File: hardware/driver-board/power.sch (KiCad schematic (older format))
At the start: 3 parts, among them U2 AIC1748

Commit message: Rework power to four different voltage domains
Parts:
- removed U2: AIC1748, Package_TO_SOT_SMD:SOT-23, symbol driver-board:AIC1748
- added C5, C6: 10µF, Capacitor_SMD:C_0603_1608Metric, symbol Device:C
- added C7: 1µF, Capacitor_SMD:C_0603_1608Metric, symbol Device:C
- added C8: 4.7µF, Capacitor_SMD:C_0603_1608Metric, symbol Device:C
- added L1: 10µH, Inductor_SMD:L_0603_1608Metric, symbol Device:L
- added R1: 1M, Resistor_SMD:R_0603_1608Metric, symbol Device:R
- added R2: 71.5k, Resistor_SMD:R_0603_1608Metric, symbol Device:R
- added U2, U3: ME6210, Package_TO_SOT_SMD:SOT-23, symbol driver-board:ME6210
- added U4: TLV61046ADB, Package_TO_SOT_SMD:SOT-23-6, symbol Regulator_Switching:TLV61046ADB
- C3, C4: value 1µF -> 10µF
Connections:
- net labels added: +12V, +3V0
- wire segments 5 -> 16

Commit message: Add display schematics
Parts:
- renumbered C5 to C3, C6 to C4, C3 to C5, C4 to C6, U3 to U2, U2 to U3
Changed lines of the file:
@@
 $Descr A4 11693 8268
 encoding utf-8
-Sheet 3 6
+Sheet 3 7
 Title "FT81x TFT040 Driver Board"
-Date "2020-07-03"
+Date "2020-07-05"
 Rev "2007D"
 Comp ""
@@
 $EndDescr
 $Comp
-L driver-board:ME6210 U2
+L driver-board:ME6210 U3
 U 1 1 5F050907
 P 4150 2150
-F 0 "U2" H 4150 2565 50  0000 C CNN
+F 0 "U3" H 4150 2565 50  0000 C CNN
 F 1 "ME6210" H 4150 2474 50  0000 C CNN
 F 2 "Package_TO_SOT_SMD:SOT-23" H 4150 1400 50  0001 C CNN
@@
 $EndComp
 $Comp
-L driver-board:ME6210 U3
+L driver-board:ME6210 U2
 U 1 1 5F051BDD
 P 7200 2100
-F 0 "U3" H 7200 2515 50  0000 C CNN
+F 0 "U2" H 7200 2515 50  0000 C CNN
 F 1 "ME6210" H 7200 2424 50  0000 C CNN
 F 2 "Package_TO_SOT_SMD:SOT-23" H 7200 1350 50  0001 C CNN
@@
 $EndComp
 $Comp
-L Device:C C3
+L Device:C C5
 U 1 1 5F05254D
 P 3500 2200
-F 0 "C3" H 3615 2246 50  0000 L CNN
+F 0 "C5" H 3615 2246 50  0000 L CNN
 F 1 "10µF" H 3615 2155 50  0000 L CNN
 F 2 "Capacitor_SMD:C_0603_1608Metric" H 3538 2050 50  0001 C CNN
@@
 $EndComp
 $Comp
-L Device:C C4
+L Device:C C6
 U 1 1 5F052D97
 P 4800 2200
-F 0 "C4" H 4915 2246 50  0000 L CNN
+F 0 "C6" H 4915 2246 50  0000 L CNN
 F 1 "10µF" H 4915 2155 50  0000 L CNN
 F 2 "Capacitor_SMD:C_0603_1608Metric" H 4838 2050 50  0001 C CNN
@@
 	3800 2050 3500 2050
 $Comp
-L power:GND #PWR017
+L power:GND #PWR018
 U 1 1 5F0548F7
 P 4150 2400
-F 0 "#PWR017" H 4150 2150 50  0001 C CNN
+F 0 "#PWR018" H 4150 2150 50  0001 C CNN
 F 1 "GND" H 4155 2227 50  0000 C CNN
 F 2 "" H 4150 2400 50  0001 C CNN
@@
 $EndComp
 $Comp
-L power:GND #PWR013
+L power:GND #PWR015
 U 1 1 5F055174
 P 3500 2350
-F 0 "#PWR013" H 3500 2100 50  0001 C CNN
+F 0 "#PWR015" H 3500 2100 50  0001 C CNN
 F 1 "GND" H 3505 2177 50  0000 C CNN
 F 2 "" H 3500 2350 50  0001 C CNN
@@
 $EndComp
 $Comp
-L power:GND #PWR014
+L power:GND #PWR016
 U 1 1 5F055676
 P 4800 2350
-F 0 "#PWR014" H 4800 2100 50  0001 C CNN
+F 0 "#PWR016" H 4800 2100 50  0001 C CNN
 F 1 "GND" H 4805 2177 50  0000 C CNN
 F 2 "" H 4800 2350 50  0001 C CNN
@@
 $EndComp
 $Comp
-L power:+3.3V #PWR010
+L power:+3.3V #PWR012
 U 1 1 5F055D4A
 P 4800 2050
-F 0 "#PWR010" H 4800 1900 50  0001 C CNN
+F 0 "#PWR012" H 4800 1900 50  0001 C CNN
 F 1 "+3.3V" H 4815 2223 50  0000 C CNN
 F 2 "" H 4800 2050 50  0001 C CNN
@@
 Connection ~ 4800 2050
 $Comp
-L power:+5V #PWR09
+L power:+5V #PWR011
 U 1 1 5F056439
 P 3500 2050
-F 0 "#PWR09" H 3500 1900 50  0001 C CNN
+F 0 "#PWR011" H 3500 1900 50  0001 C CNN
 F 1 "+5V" H 3515 2223 50  0000 C CNN
 F 2 "" H 3500 2050 50  0001 C CNN
@@
 Connection ~ 3500 2050
 $Comp
-L Device:C C5
+L Device:C C3
 U 1 1 5F057FFE
 P 6550 2150
-F 0 "C5" H 6665 2196 50  0000 L CNN
+F 0 "C3" H 6665 2196 50  0000 L CNN
 F 1 "10µF" H 6665 2105 50  0000 L CNN
 F 2 "Capacitor_SMD:C_0603_1608Metric" H 6588 2000 50  0001 C CNN
@@
 $EndComp
 $Comp
-L Device:C C6
+L Device:C C4
 U 1 1 5F058C7E
 P 7850 2150
-F 0 "C6" H 7965 2196 50  0000 L CNN
+F 0 "C4" H 7965 2196 50  0000 L CNN
 F 1 "10µF" H 7965 2105 50  0000 L CNN
 F 2 "Capacitor_SMD:C_0603_1608Metric" H 7888 2000 50  0001 C CNN
@@
 	7550 2000 7850 2000
 $Comp
-L power:GND #PWR016
+L power:GND #PWR014
 U 1 1 5F05A343
 P 7850 2300
-F 0 "#PWR016" H 7850 2050 50  0001 C CNN
+F 0 "#PWR014" H 7850 2050 50  0001 C CNN
 F 1 "GND" H 7855 2127 50  0000 C CNN
 F 2 "" H 7850 2300 50  0001 C CNN
@@
 $EndComp
 $Comp
-L power:GND #PWR018
+L power:GND #PWR017
 U 1 1 5F05A491
 P 7200 2350
-F 0 "#PWR018" H 7200 2100 50  0001 C CNN
+F 0 "#PWR017" H 7200 2100 50  0001 C CNN
 F 1 "GND" H 7205 2177 50  0000 C CNN
 F 2 "" H 7200 2350 50  0001 C CNN
@@
 $EndComp
 $Comp
-L power:GND #PWR015
+L power:GND #PWR013
 U 1 1 5F05A5EB
 P 6550 2300
-F 0 "#PWR015" H 6550 2050 50  0001 C CNN
+F 0 "#PWR013" H 6550 2050 50  0001 C CNN
 F 1 "GND" H 6555 2127 50  0000 C CNN
 F 2 "" H 6550 2300 50  0001 C CNN
@@
 $EndComp
 $Comp
-L power:+5V #PWR011
+L power:+5V #PWR09
 U 1 1 5F05A77C
 P 6550 2000
-F 0 "#PWR011" H 6550 1850 50  0001 C CNN
+F 0 "#PWR09" H 6550 1850 50  0001 C CNN
 F 1 "+5V" H 6565 2173 50  0000 C CNN
 F 2 "" H 6550 2000 50  0001 C CNN
@@
 Connection ~ 6550 2000
 $Comp
-L power:+3V0 #PWR012
+L power:+3V0 #PWR010
 U 1 1 5F05A91B
 P 7850 2000
-F 0 "#PWR012" H 7850 1850 50  0001 C CNN
+F 0 "#PWR010" H 7850 1850 50  0001 C CNN
 F 1 "+3V0" H 7865 2173 50  0000 C CNN
 F 2 "" H 7850 2000 50  0001 C CNN

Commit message: Improve and fix pcb and schematic
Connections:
- net +12V: now also U4.5 (VOUT); no longer R2.1, U4.3 (FB)
- net at R1.2: now also R2.1, U4.3 (FB); no longer U4.5 (VOUT)
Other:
- moved on the sheet: C8, R2
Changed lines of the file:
@@
 $EndComp
-$Comp
-L Device:R R1
-U 1 1 5F06FAA8
-P 6350 4250
-F 0 "R1" V 6250 4250 50  0000 C CNN
-F 1 "1M" V 6350 4250 50  0000 C CNN
-F 2 "Resistor_SMD:R_0603_1608Metric" V 6280 4250 50  0001 C CNN
-F 3 "~" H 6350 4250 50  0001 C CNN
-	1    6350 4250
-	0    1    1    0
-$EndComp
-Wire Wire Line
-	6050 4250 6200 4250
 $Comp
 L Device:R R2
 U 1 1 5F07151B
-P 6500 4600
-F 0 "R2" H 6570 4646 50  0000 L CNN
-F 1 "71.5k" H 6570 4555 50  0000 L CNN
-F 2 "Resistor_SMD:R_0603_1608Metric" V 6430 4600 50  0001 C CNN
-F 3 "~" H 6500 4600 50  0001 C CNN
-	1    6500 4600
+P 6400 4800
+F 0 "R2" H 6470 4846 50  0000 L CNN
+F 1 "71.5k" H 6470 4755 50  0000 L CNN
+F 2 "Resistor_SMD:R_0603_1608Metric" V 6330 4800 50  0001 C CNN
+F 3 "~" H 6400 4800 50  0001 C CNN
+	1    6400 4800
 	1    0    0    -1
 $EndComp
-Wire Wire Line
-	6500 4250 6500 4350
-Wire Wire Line
-	6050 4350 6500 4350
-Connection ~ 6500 4350
-Wire Wire Line
-	6500 4350 6500 4450
 $Comp
 L power:GND #PWR025
 U 1 1 5F072953
-P 6500 4750
-F 0 "#PWR025" H 6500 4500 50  0001 C CNN
-F 1 "GND" H 6505 4577 50  0000 C CNN
-F 2 "" H 6500 4750 50  0001 C CNN
-F 3 "" H 6500 4750 50  0001 C CNN
-	1    6500 4750
+P 6400 4950
+F 0 "#PWR025" H 6400 4700 50  0001 C CNN
+F 1 "GND" H 6405 4777 50  0000 C CNN
+F 2 "" H 6400 4950 50  0001 C CNN
+F 3 "" H 6400 4950 50  0001 C CNN
+	1    6400 4950
 	1    0    0    -1
 $EndComp
@@
 L Device:C C8
 U 1 1 5F07504E
-P 7000 4400
-F 0 "C8" H 7115 4446 50  0000 L CNN
-F 1 "4.7µF" H 7115 4355 50  0000 L CNN
-F 2 "Capacitor_SMD:C_0603_1608Metric" H 7038 4250 50  0001 C CNN
-F 3 "~" H 7000 4400 50  0001 C CNN
-	1    7000 4400
+P 6800 4400
+F 0 "C8" H 6915 4446 50  0000 L CNN
+F 1 "4.7µF" H 6915 4355 50  0000 L CNN
+F 2 "Capacitor_SMD:C_0603_1608Metric" H 6838 4250 50  0001 C CNN
+F 3 "~" H 6800 4400 50  0001 C CNN
+	1    6800 4400
 	1    0    0    -1
 $EndComp
-Wire Wire Line
-	6500 4250 7000 4250
-Connection ~ 6500 4250
 $Comp
 L power:GND #PWR024
 U 1 1 5F076C9E
-P 7000 4550
-F 0 "#PWR024" H 7000 4300 50  0001 C CNN
-F 1 "GND" H 7005 4377 50  0000 C CNN
-F 2 "" H 7000 4550 50  0001 C CNN
-F 3 "" H 7000 4550 50  0001 C CNN
-	1    7000 4550
+P 6800 4550
+F 0 "#PWR024" H 6800 4300 50  0001 C CNN
+F 1 "GND" H 6805 4377 50  0000 C CNN
+F 2 "" H 6800 4550 50  0001 C CNN
+F 3 "" H 6800 4550 50  0001 C CNN
+	1    6800 4550
 	1    0    0    -1
 $EndComp
@@
 L power:+12V #PWR020
 U 1 1 5F07735E
-P 7000 4250
-F 0 "#PWR020" H 7000 4100 50  0001 C CNN
-F 1 "+12V" H 7015 4423 50  0000 C CNN
-F 2 "" H 7000 4250 50  0001 C CNN
-F 3 "" H 7000 4250 50  0001 C CNN
-	1    7000 4250
+P 6800 4250
+F 0 "#PWR020" H 6800 4100 50  0001 C CNN
+F 1 "+12V" H 6815 4423 50  0000 C CNN
+F 2 "" H 6800 4250 50  0001 C CNN
+F 3 "" H 6800 4250 50  0001 C CNN
+	1    6800 4250
 	1    0    0    -1
 $EndComp
-Connection ~ 7000 4250
 $Comp
 L Device:L L1
@@
 Wire Wire Line
 	5350 4150 4800 4150
+$Comp
+L Device:R R1
+U 1 1 5F0697E7
+P 6400 4400
+F 0 "R1" H 6470 4446 50  0000 L CNN
+F 1 "1M" H 6470 4355 50  0000 L CNN
+F 2 "Resistor_SMD:R_0603_1608Metric" V 6330 4400 50  0001 C CNN
+F 3 "~" H 6400 4400 50  0001 C CNN
+	1    6400 4400
+	1    0    0    -1
+$EndComp
+Wire Wire Line
+	6050 4250 6400 4250
+Connection ~ 6800 4250
+Connection ~ 6400 4250
+Wire Wire Line
+	6400 4250 6800 4250
+Wire Wire Line
+	6400 4550 6400 4600
+Wire Wire Line
+	6050 4350 6150 4350
+Wire Wire Line
+	6150 4350 6150 4600
+Wire Wire Line
+	6150 4600 6400 4600
+Connection ~ 6400 4600
+Wire Wire Line
+	6400 4600 6400 4650
 $EndSCHEMATC

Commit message: Add missing JLCPCB part numbers
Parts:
- C3, C4, C5, C6: JLCPCB (none) -> C19702
- C7: JLCPCB (none) -> C15849
- R2: JLCPCB (none) -> C23103
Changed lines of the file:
@@
 F 2 "Capacitor_SMD:C_0603_1608Metric" H 3538 2050 50  0001 C CNN
 F 3 "~" H 3500 2200 50  0001 C CNN
+F 4 "C19702" H 3500 2200 50  0001 C CNN "JLCPCB"
 	1    3500 2200
 	1    0    0    -1
@@
 F 2 "Capacitor_SMD:C_0603_1608Metric" H 4838 2050 50  0001 C CNN
 F 3 "~" H 4800 2200 50  0001 C CNN
+F 4 "C19702" H 4800 2200 50  0001 C CNN "JLCPCB"
 	1    4800 2200
 	1    0    0    -1
@@
 F 2 "Capacitor_SMD:C_0603_1608Metric" H 6588 2000 50  0001 C CNN
 F 3 "~" H 6550 2150 50  0001 C CNN
+F 4 "C19702" H 6550 2150 50  0001 C CNN "JLCPCB"
 	1    6550 2150
 	1    0    0    -1
@@
 F 2 "Capacitor_SMD:C_0603_1608Metric" H 7888 2000 50  0001 C CNN
 F 3 "~" H 7850 2150 50  0001 C CNN
+F 4 "C19702" H 7850 2150 50  0001 C CNN "JLCPCB"
 	1    7850 2150
 	1    0    0    -1
@@
 F 2 "Capacitor_SMD:C_0603_1608Metric" H 4838 4150 50  0001 C CNN
 F 3 "~" H 4800 4300 50  0001 C CNN
+F 4 "C15849" H 4800 4300 50  0001 C CNN "JLCPCB"
 	1    4800 4300
 	1    0    0    -1
@@
 F 2 "Resistor_SMD:R_0603_1608Metric" V 6330 4800 50  0001 C CNN
 F 3 "~" H 6400 4800 50  0001 C CNN
+F 4 "C23103" H 6400 4800 50  0001 C CNN "JLCPCB"
 	1    6400 4800
 	1    0    0    -1

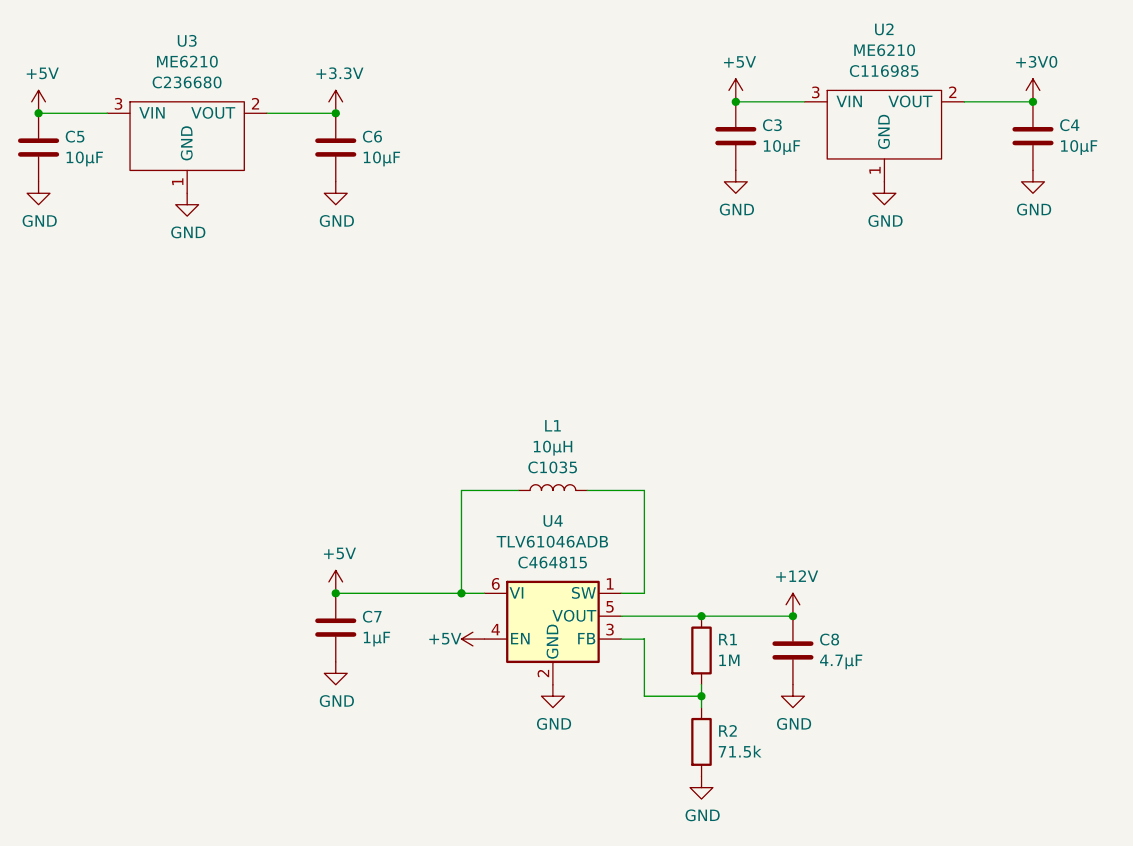
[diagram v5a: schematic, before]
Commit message: Rename JLCPCB to LCSC and update PCB
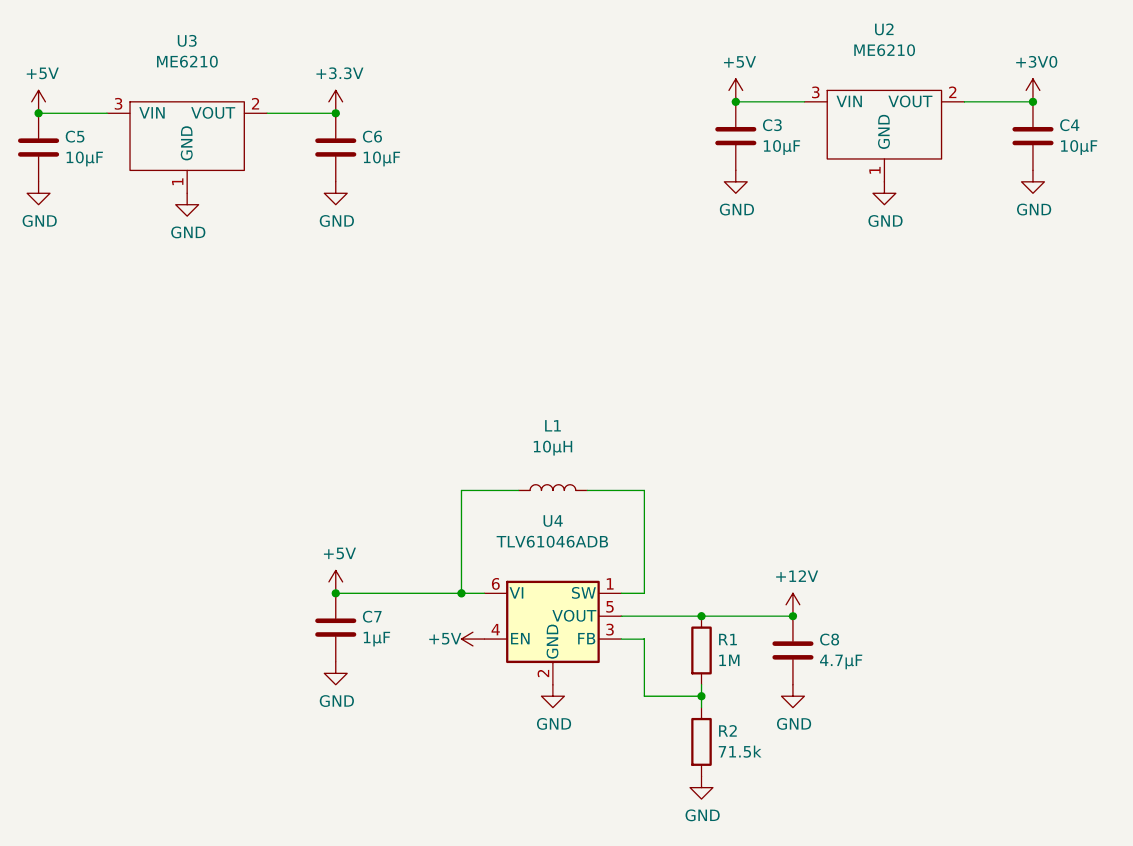
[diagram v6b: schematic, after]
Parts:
- C3, C4, C5, C6: JLCPCB C19702 -> (none); LCSC (none) -> C19702
- C7: JLCPCB C15849 -> (none); LCSC (none) -> C15849
- C8: LCSC (none) -> C19666
- L1: JLCPCB C1035 -> (none); LCSC (none) -> C1035
- R1: LCSC (none) -> C22935
- R2: JLCPCB C23103 -> (none); LCSC (none) -> C23103
- U2: JLCPCB C116985 -> (none); LCSC (none) -> C116985
- U3: JLCPCB C236680 -> (none); LCSC (none) -> C236680
- U4: JLCPCB C464815 -> (none); LCSC (none) -> C464815
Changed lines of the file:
@@
 F 2 "Package_TO_SOT_SMD:SOT-23" H 4150 1400 50  0001 C CNN
 F 3 "" H 4150 2150 50  0001 C CNN
-F 4 "C236680" H 4150 2383 50  0000 C CNN "JLCPCB"
+F 4 "C236680" H 4150 2150 50  0001 C CNN "LCSC"
 	1    4150 2150
 	1    0    0    -1
@@
 F 2 "Package_TO_SOT_SMD:SOT-23" H 7200 1350 50  0001 C CNN
 F 3 "" H 7200 2100 50  0001 C CNN
-F 4 "C116985" H 7200 2333 50  0000 C CNN "JLCPCB"
+F 4 "C116985" H 7200 2100 50  0001 C CNN "LCSC"
 	1    7200 2100
 	1    0    0    -1
@@
 F 2 "Capacitor_SMD:C_0603_1608Metric" H 3538 2050 50  0001 C CNN
 F 3 "~" H 3500 2200 50  0001 C CNN
-F 4 "C19702" H 3500 2200 50  0001 C CNN "JLCPCB"
+F 4 "C19702" H 3500 2200 50  0001 C CNN "LCSC"
 	1    3500 2200
 	1    0    0    -1
@@
 F 2 "Capacitor_SMD:C_0603_1608Metric" H 4838 2050 50  0001 C CNN
 F 3 "~" H 4800 2200 50  0001 C CNN
-F 4 "C19702" H 4800 2200 50  0001 C CNN "JLCPCB"
+F 4 "C19702" H 4800 2200 50  0001 C CNN "LCSC"
 	1    4800 2200
 	1    0    0    -1
@@
 F 2 "Capacitor_SMD:C_0603_1608Metric" H 6588 2000 50  0001 C CNN
 F 3 "~" H 6550 2150 50  0001 C CNN
-F 4 "C19702" H 6550 2150 50  0001 C CNN "JLCPCB"
+F 4 "C19702" H 6550 2150 50  0001 C CNN "LCSC"
 	1    6550 2150
 	1    0    0    -1
@@
 F 2 "Capacitor_SMD:C_0603_1608Metric" H 7888 2000 50  0001 C CNN
 F 3 "~" H 7850 2150 50  0001 C CNN
-F 4 "C19702" H 7850 2150 50  0001 C CNN "JLCPCB"
+F 4 "C19702" H 7850 2150 50  0001 C CNN "LCSC"
 	1    7850 2150
 	1    0    0    -1
@@
 F 2 "Package_TO_SOT_SMD:SOT-23-6" H 5800 4200 50  0001 L CIN
 F 3 "http://www.ti.com/lit/ds/symlink/tlv61046a.pdf" H 5750 4450 50  0001 C CNN
-F 4 "C464815" H 5750 4683 50  0000 C CNN "JLCPCB"
+F 4 "C464815" H 5750 4350 50  0001 C CNN "LCSC"
 	1    5750 4350
 	1    0    0    -1
@@
 F 2 "Capacitor_SMD:C_0603_1608Metric" H 4838 4150 50  0001 C CNN
 F 3 "~" H 4800 4300 50  0001 C CNN
-F 4 "C15849" H 4800 4300 50  0001 C CNN "JLCPCB"
+F 4 "C15849" H 4800 4300 50  0001 C CNN "LCSC"
 	1    4800 4300
 	1    0    0    -1
@@
 F 2 "Resistor_SMD:R_0603_1608Metric" V 6330 4800 50  0001 C CNN
 F 3 "~" H 6400 4800 50  0001 C CNN
-F 4 "C23103" H 6400 4800 50  0001 C CNN "JLCPCB"
+F 4 "C23103" H 6400 4800 50  0001 C CNN "LCSC"
 	1    6400 4800
 	1    0    0    -1
@@
 F 2 "Capacitor_SMD:C_0603_1608Metric" H 6838 4250 50  0001 C CNN
 F 3 "~" H 6800 4400 50  0001 C CNN
+F 4 "C19666" H 6800 4400 50  0001 C CNN "LCSC"
 	1    6800 4400
 	1    0    0    -1
@@
 F 2 "Inductor_SMD:L_0603_1608Metric" H 5750 3700 50  0001 C CNN
 F 3 "~" H 5750 3700 50  0001 C CNN
-F 4 "C1035" V 5849 3700 50  0000 C CNN "JLCPCB"
+F 4 "C1035" H 5750 3700 50  0001 C CNN "LCSC"
 	1    5750 3700
 	0    -1   -1   0
@@
 F 2 "Resistor_SMD:R_0603_1608Metric" V 6330 4400 50  0001 C CNN
 F 3 "~" H 6400 4400 50  0001 C CNN
+F 4 "C22935" H 6400 4400 50  0001 C CNN "LCSC"
 	1    6400 4400
 	1    0    0    -1
